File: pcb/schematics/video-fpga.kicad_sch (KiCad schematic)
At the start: 60 parts, among them J5 Conn_01x06, J6 Conn_01x06, U4 LCMXO2-7000HC-4TG144C, X1 ASV-xxxMHz

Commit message: place components around connectors
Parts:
- X1: Part Number (none) -> ASV-40.000MHZ-EJ-T
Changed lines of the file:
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@@
+      (effects (font (size 1.27 1.27)) hide)
+    )
+    (property "Part Number" "ASV-40.000MHZ-EJ-T" (id 4) (at 127 176.53 0)
       (effects (font (size 1.27 1.27)) hide)
     )

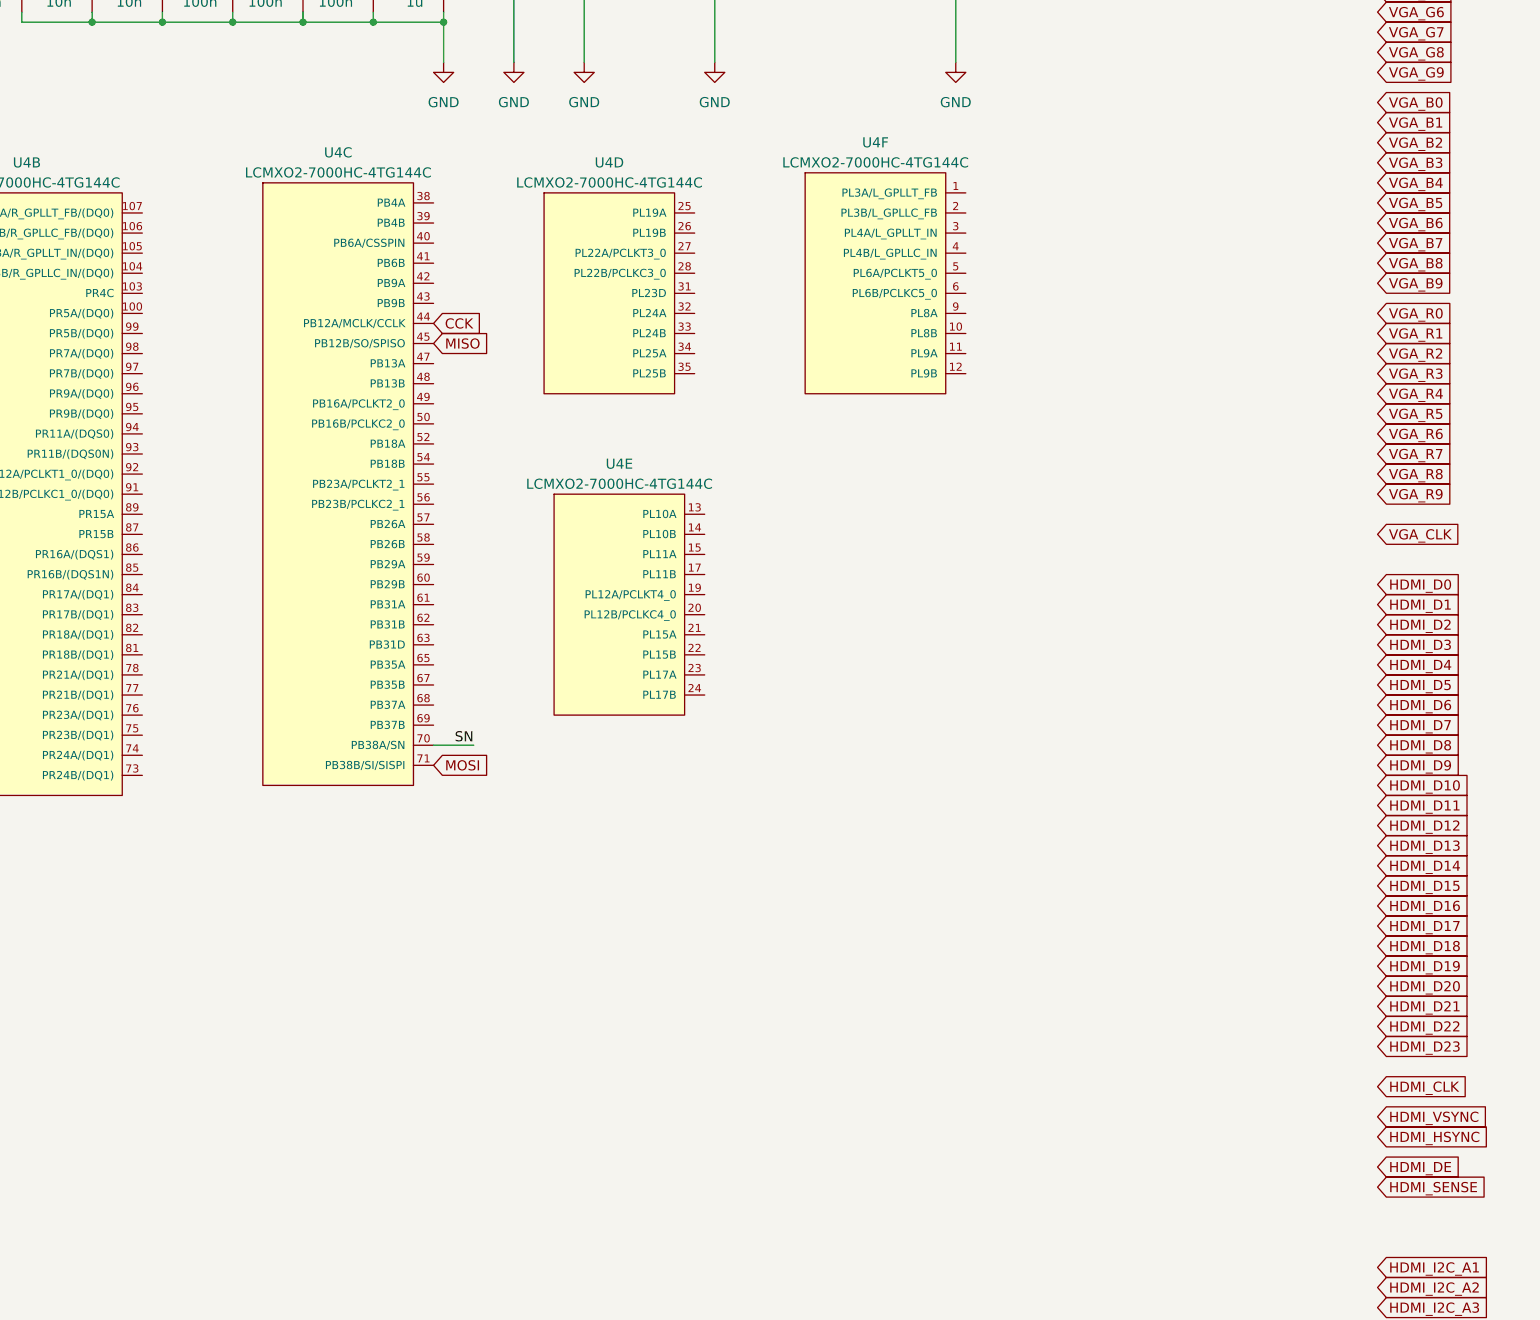
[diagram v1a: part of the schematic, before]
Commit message: add traces for hdmi interface with proper anti crosstalk
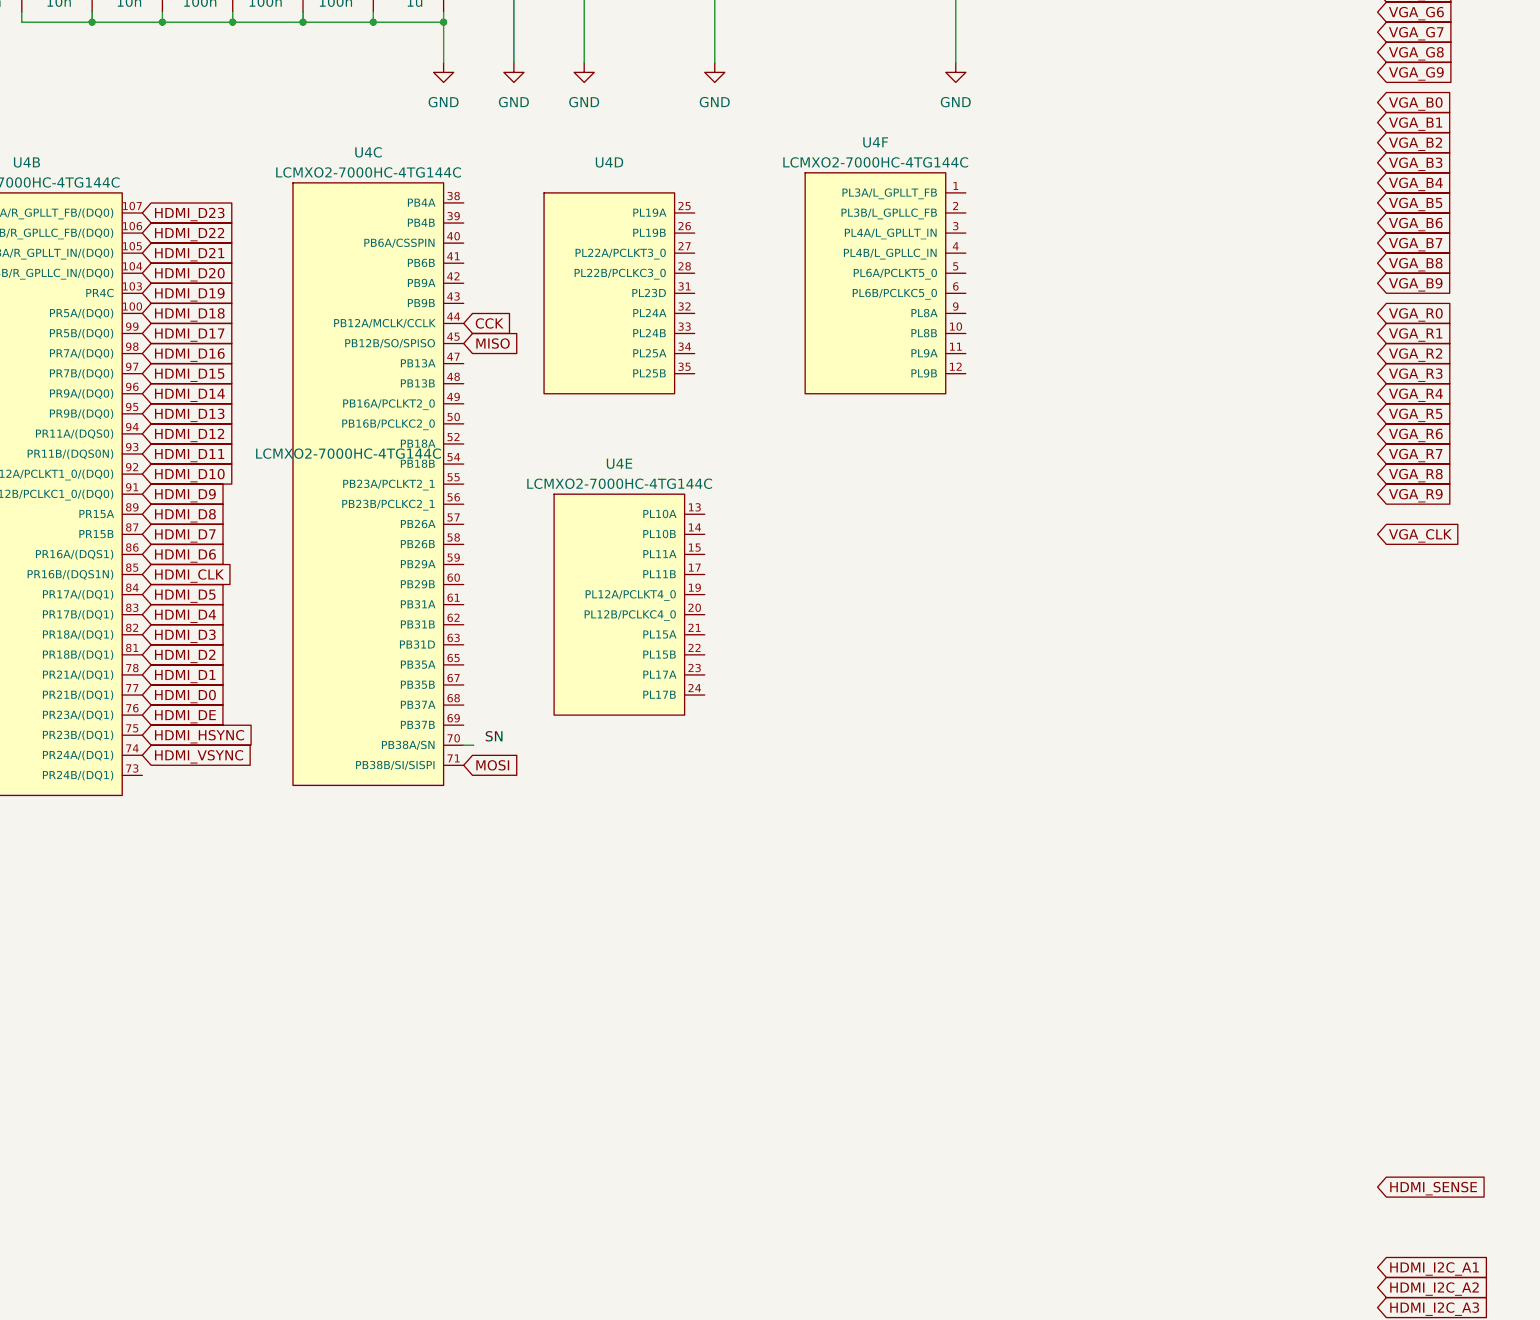
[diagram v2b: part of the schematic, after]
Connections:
- net HDMI_CLK: now also U4.85 (PR16B/(DQS1N))
- net HDMI_D0: now also U4.77 (PR21B/(DQ1))
- net HDMI_D1: now also U4.78 (PR21A/(DQ1))
- net HDMI_D10: now also U4.92 (PR12A/PCLKT1_0/(DQ0))
- net HDMI_D11: now also U4.93 (PR11B/(DQS0N))
- net HDMI_D12: now also U4.94 (PR11A/(DQS0))
- net HDMI_D13: now also U4.95 (PR9B/(DQ0))
- net HDMI_D14: now also U4.96 (PR9A/(DQ0))
- net HDMI_D15: now also U4.97 (PR7B/(DQ0))
- net HDMI_D16: now also U4.98 (PR7A/(DQ0))
- net HDMI_D17: now also U4.99 (PR5B/(DQ0))
- net HDMI_D18: now also U4.100 (PR5A/(DQ0))
- net HDMI_D19: now also U4.103 (PR4C)
- net HDMI_D2: now also U4.81 (PR18B/(DQ1))
- net HDMI_D20: now also U4.104 (PR3B/R_GPLLC_IN/(DQ0))
- net HDMI_D21: now also U4.105 (PR3A/R_GPLLT_IN/(DQ0))
- net HDMI_D22: now also U4.106 (PR2B/R_GPLLC_FB/(DQ0))
- net HDMI_D23: now also U4.107 (PR2A/R_GPLLT_FB/(DQ0))
- net HDMI_D3: now also U4.82 (PR18A/(DQ1))
- net HDMI_D4: now also U4.83 (PR17B/(DQ1))
- net HDMI_D5: now also U4.84 (PR17A/(DQ1))
- net HDMI_D6: now also U4.86 (PR16A/(DQS1))
- net HDMI_D7: now also U4.87 (PR15B)
- net HDMI_D8: now also U4.89 (PR15A)
- net HDMI_D9: now also U4.91 (PR12B/PCLKC1_0/(DQ0))
- net HDMI_DE: now also U4.76 (PR23A/(DQ1))
- net HDMI_HSYNC: now also U4.75 (PR23B/(DQ1))
- net HDMI_VSYNC: now also U4.74 (PR24A/(DQ1))
- net SN: no longer U4.70 (PB38A/SN)
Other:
- moved on the sheet: U4C

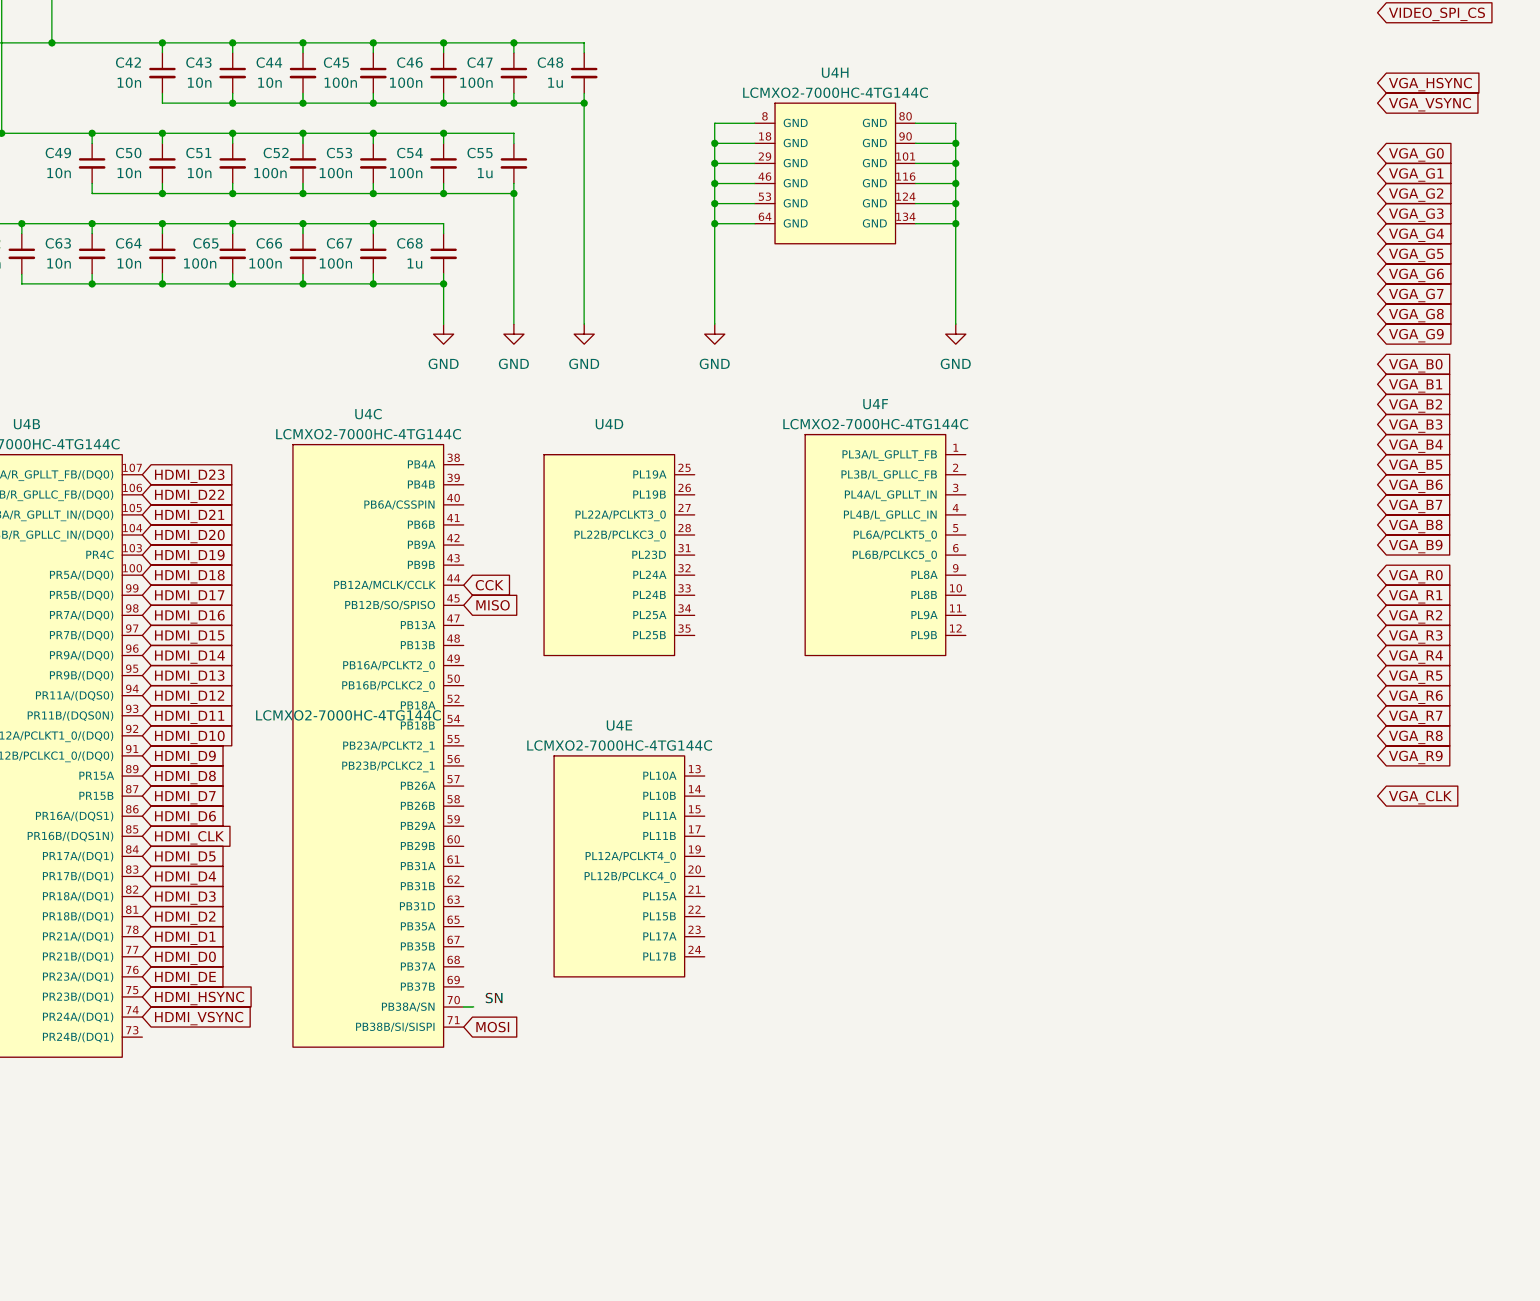
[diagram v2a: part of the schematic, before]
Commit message: change the bank for the hdmi interface
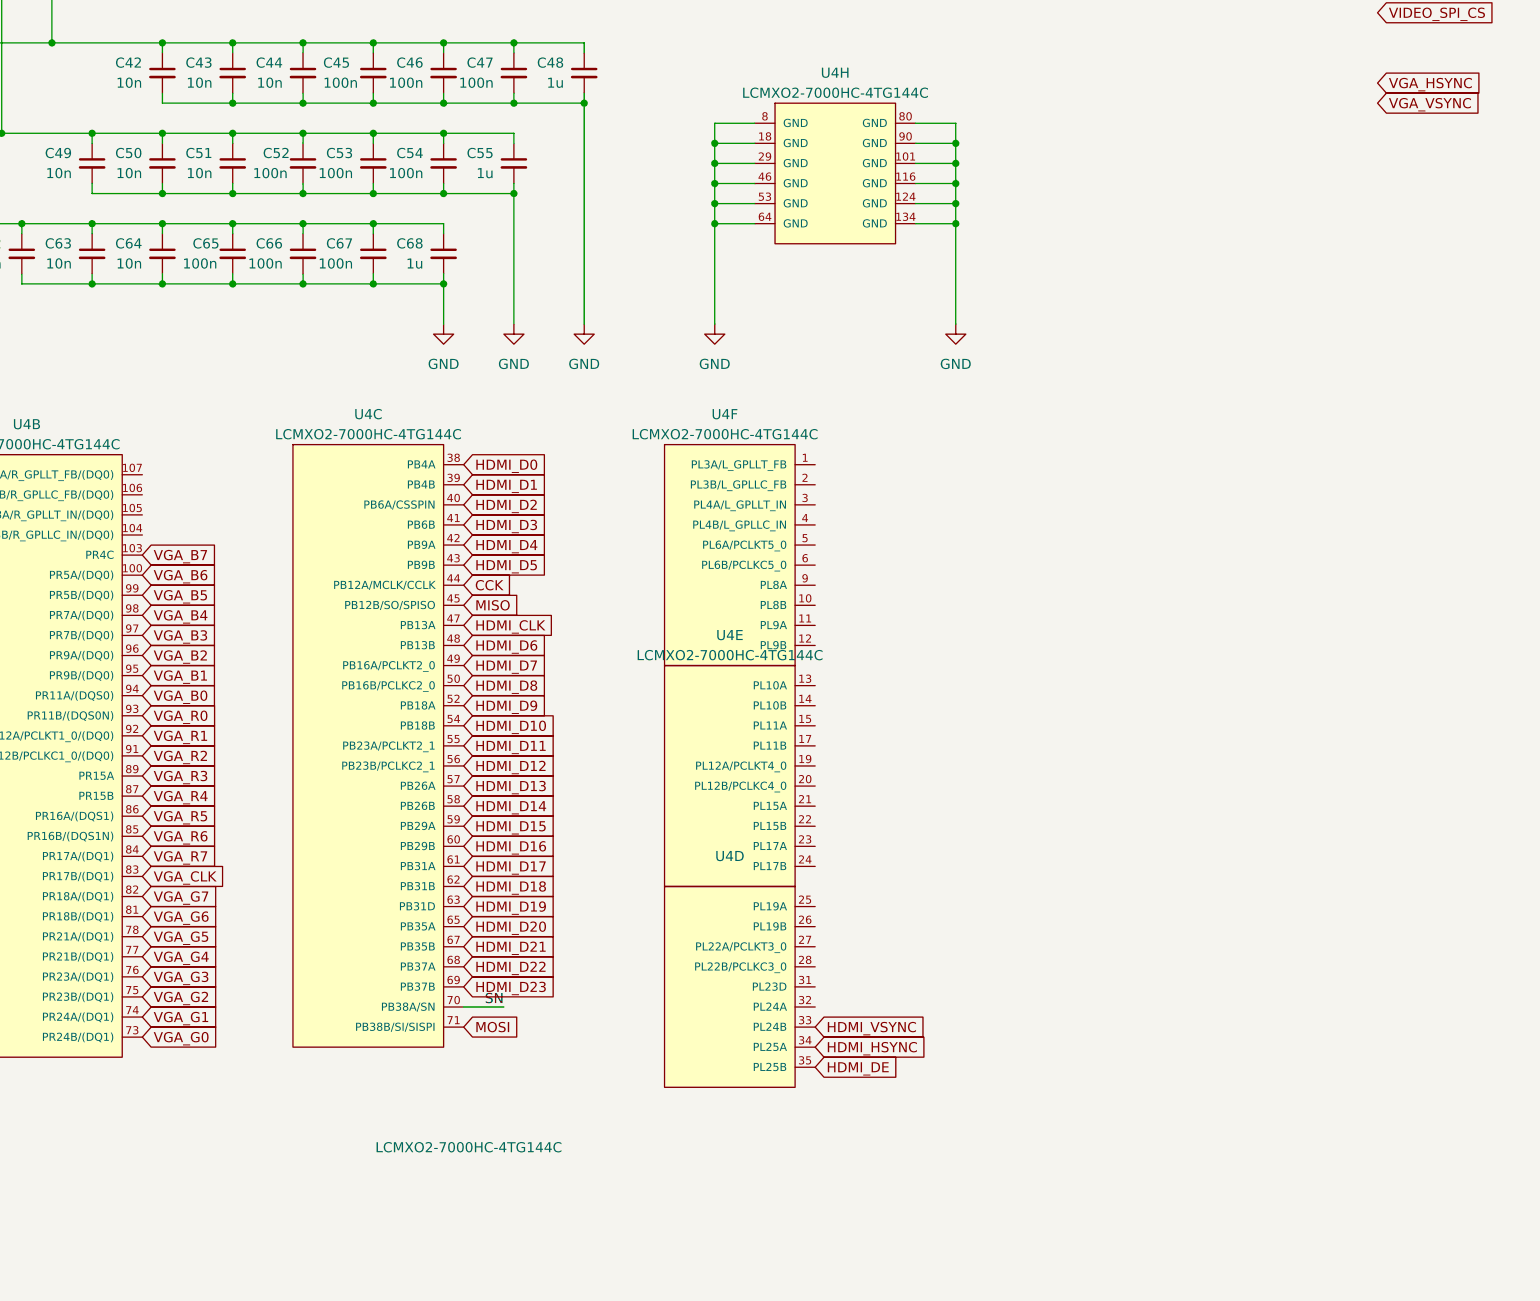
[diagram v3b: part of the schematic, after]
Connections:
- net HDMI_CLK: now also U4.47 (PB13A); no longer U4.85 (PR16B/(DQS1N))
- net HDMI_D0: now also U4.38 (PB4A); no longer U4.77 (PR21B/(DQ1))
- net HDMI_D1: now also U4.39 (PB4B); no longer U4.78 (PR21A/(DQ1))
- net HDMI_D10: now also U4.54 (PB18B); no longer U4.92 (PR12A/PCLKT1_0/(DQ0))
- net HDMI_D11: now also U4.55 (PB23A/PCLKT2_1); no longer U4.93 (PR11B/(DQS0N))
- net HDMI_D12: now also U4.56 (PB23B/PCLKC2_1); no longer U4.94 (PR11A/(DQS0))
- net HDMI_D13: now also U4.57 (PB26A); no longer U4.95 (PR9B/(DQ0))
- net HDMI_D14: now also U4.58 (PB26B); no longer U4.96 (PR9A/(DQ0))
- net HDMI_D15: now also U4.59 (PB29A); no longer U4.97 (PR7B/(DQ0))
- net HDMI_D16: now also U4.60 (PB29B); no longer U4.98 (PR7A/(DQ0))
- net HDMI_D17: now also U4.61 (PB31A); no longer U4.99 (PR5B/(DQ0))
- net HDMI_D18: now also U4.62 (PB31B); no longer U4.100 (PR5A/(DQ0))
- net HDMI_D19: now also U4.63 (PB31D); no longer U4.103 (PR4C)
- net HDMI_D2: now also U4.40 (PB6A/CSSPIN); no longer U4.81 (PR18B/(DQ1))
- net HDMI_D20: now also U4.65 (PB35A); no longer U4.104 (PR3B/R_GPLLC_IN/(DQ0))
- net HDMI_D21: now also U4.67 (PB35B); no longer U4.105 (PR3A/R_GPLLT_IN/(DQ0))
- net HDMI_D22: now also U4.68 (PB37A); no longer U4.106 (PR2B/R_GPLLC_FB/(DQ0))
- net HDMI_D23: now also U4.69 (PB37B); no longer U4.107 (PR2A/R_GPLLT_FB/(DQ0))
- net HDMI_D3: now also U4.41 (PB6B); no longer U4.82 (PR18A/(DQ1))
- net HDMI_D4: now also U4.42 (PB9A); no longer U4.83 (PR17B/(DQ1))
- net HDMI_D5: now also U4.43 (PB9B); no longer U4.84 (PR17A/(DQ1))
- net HDMI_D6: now also U4.48 (PB13B); no longer U4.86 (PR16A/(DQS1))
- net HDMI_D7: now also U4.49 (PB16A/PCLKT2_0); no longer U4.87 (PR15B)
- net HDMI_D8: now also U4.50 (PB16B/PCLKC2_0); no longer U4.89 (PR15A)
- net HDMI_D9: now also U4.52 (PB18A); no longer U4.91 (PR12B/PCLKC1_0/(DQ0))
- net HDMI_DE: now also U4.35 (PL25B); no longer U4.76 (PR23A/(DQ1))
- net HDMI_HSYNC: now also U4.34 (PL25A); no longer U4.75 (PR23B/(DQ1))
- net HDMI_VSYNC: now also U4.33 (PL24B); no longer U4.74 (PR24A/(DQ1))
- net SN: now also U4.70 (PB38A/SN)
- net VGA_B0: now also U4.94 (PR11A/(DQS0))
- net VGA_B1: now also U4.95 (PR9B/(DQ0))
- net VGA_B2: now also U4.96 (PR9A/(DQ0))
- net VGA_B3: now also U4.97 (PR7B/(DQ0))
- net VGA_B4: now also U4.98 (PR7A/(DQ0))
- net VGA_B5: now also U4.99 (PR5B/(DQ0))
- net VGA_B6: now also U4.100 (PR5A/(DQ0))
- net VGA_B7: now also U4.103 (PR4C)
- net VGA_CLK: now also U4.83 (PR17B/(DQ1))
- net VGA_G0: now also U4.73 (PR24B/(DQ1))
- net VGA_G1: now also U4.74 (PR24A/(DQ1))
- net VGA_G2: now also U4.75 (PR23B/(DQ1))
- net VGA_G3: now also U4.76 (PR23A/(DQ1))
- net VGA_G4: now also U4.77 (PR21B/(DQ1))
- net VGA_G5: now also U4.78 (PR21A/(DQ1))
- net VGA_G6: now also U4.81 (PR18B/(DQ1))
- net VGA_G7: now also U4.82 (PR18A/(DQ1))
- net VGA_R0: now also U4.93 (PR11B/(DQS0N))
- net VGA_R1: now also U4.92 (PR12A/PCLKT1_0/(DQ0))
- net VGA_R2: now also U4.91 (PR12B/PCLKC1_0/(DQ0))
- net VGA_R3: now also U4.89 (PR15A)
- net VGA_R4: now also U4.87 (PR15B)
- net VGA_R5: now also U4.86 (PR16A/(DQS1))
- net VGA_R6: now also U4.85 (PR16B/(DQS1N))
- net VGA_R7: now also U4.84 (PR17A/(DQ1))
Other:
- moved on the sheet: U4D, U4E, U4F
